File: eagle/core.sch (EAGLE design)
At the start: 28 parts, among them T1 BC846, T2 BC846, T3 BC846, T4 BC846

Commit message: Added capacitor between 3v and gnd on core pcb
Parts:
- added C3: 0.1u, resistor:C-EUC0805
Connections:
- net 3V: now also C3.1
- net GND: now also C3.2
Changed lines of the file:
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@@
 <part name="R11" library="resistor" library_urn="urn:adsk.eagle:library:348" deviceset="R-EU_" device="R0805" package3d_urn="urn:adsk.eagle:package:23553/2"/>
 <part name="R12" library="resistor" library_urn="urn:adsk.eagle:library:348" deviceset="R-EU_" device="R0805" package3d_urn="urn:adsk.eagle:package:23553/2"/>
+<part name="C3" library="resistor" library_urn="urn:adsk.eagle:library:348" deviceset="C-EU" device="C0805" package3d_urn="urn:adsk.eagle:package:23617/2" value="0.1u"/>
 </parts>
 <sheets>
@@
 <attribute name="VALUE" x="-22.098" y="13.97" size="1.778" layer="96" rot="R90"/>
 </instance>
+<instance part="C3" gate="G$1" x="20.32" y="30.48" smashed="yes">
+<attribute name="NAME" x="21.844" y="30.861" size="1.778" layer="95"/>
+<attribute name="VALUE" x="21.844" y="25.781" size="1.778" layer="96"/>
+</instance>
 </instances>
 <busses>
@@
 <wire x1="-144.78" y1="-27.94" x2="-139.7" y2="-27.94" width="0.1524" layer="91"/>
 <label x="-139.7" y="-27.94" size="1.778" layer="95"/>
+</segment>
+<segment>
+<pinref part="C3" gate="G$1" pin="2"/>
+<wire x1="20.32" y1="25.4" x2="25.4" y2="25.4" width="0.1524" layer="91"/>
+<label x="25.4" y="22.86" size="1.778" layer="95"/>
 </segment>
 </net>
@@
 <label x="-40.64" y="22.86" size="1.778" layer="95"/>
 </segment>
+<segment>
+<wire x1="20.32" y1="33.02" x2="15.24" y2="33.02" width="0.1524" layer="91"/>
+<pinref part="C3" gate="G$1" pin="1"/>
+<label x="12.7" y="33.02" size="1.778" layer="95"/>
+</segment>
 </net>

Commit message: Experimental fix for tft crash.
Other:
- note added: "I2C pullups"
- note removed: "Optional I2C pullups"
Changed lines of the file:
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@@
 <text x="-48.26" y="83.82" size="1.778" layer="91">Teensy 4</text>
 <text x="20.32" y="83.82" size="1.778" layer="91">Teensy 3.2</text>
-<text x="-40.64" y="25.4" size="1.778" layer="91">Optional I2C pullups</text>
+<text x="-40.64" y="25.4" size="1.778" layer="91">I2C pullups</text>
 </plain>
 <instances>

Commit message: misc pcb changes
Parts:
- removed C1, C2: 0.1u, resistor:C-EUC0805
- removed R10, R5, R8, R9: 10k, resistor:R-EU_M0805
- added GND: TPTP14R, testpad:TPTP14R
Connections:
- removed net ENCL: ENCL.TP, R5.2, R8.1
- removed net ENCR: ENCR.TP, R10.2, R9.1
- net 3V: no longer R8.2, R9.2
- net ENCPINL: now also ENCL.TP; no longer C1.1, R5.1
- net ENCPINR: now also ENCR.TP; no longer C2.1, R10.1
- net GND: now also GND.TP; no longer C1.2, C2.2
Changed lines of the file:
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@@
 </classes>
 <parts>
-<part name="R5" library="resistor" library_urn="urn:adsk.eagle:library:348" deviceset="R-EU_" device="M0805" package3d_urn="urn:adsk.eagle:package:23556/2" value="10k"/>
-<part name="R8" library="resistor" library_urn="urn:adsk.eagle:library:348" deviceset="R-EU_" device="M0805" package3d_urn="urn:adsk.eagle:package:23556/2" value="10k"/>
-<part name="R9" library="resistor" library_urn="urn:adsk.eagle:library:348" deviceset="R-EU_" device="M0805" package3d_urn="urn:adsk.eagle:package:23556/2" value="10k"/>
-<part name="R10" library="resistor" library_urn="urn:adsk.eagle:library:348" deviceset="R-EU_" device="M0805" package3d_urn="urn:adsk.eagle:package:23556/2" value="10k"/>
-<part name="C1" library="resistor" library_urn="urn:adsk.eagle:library:348" deviceset="C-EU" device="C0805" package3d_urn="urn:adsk.eagle:package:23617/2" value="0.1u"/>
-<part name="C2" library="resistor" library_urn="urn:adsk.eagle:library:348" deviceset="C-EU" device="C0805" package3d_urn="urn:adsk.eagle:package:23617/2" value="0.1u"/>
 <part name="U$1" library="general" deviceset="TEENSYSMALL" device="" value="TEENSY4"/>
 <part name="U$2" library="general" deviceset="TEENSYSMALL" device=""/>
@@
 <part name="R12" library="resistor" library_urn="urn:adsk.eagle:library:348" deviceset="R-EU_" device="R0805" package3d_urn="urn:adsk.eagle:package:23553/2"/>
 <part name="C3" library="resistor" library_urn="urn:adsk.eagle:library:348" deviceset="C-EU" device="C0805" package3d_urn="urn:adsk.eagle:package:23617/2" value="0.1u"/>
+<part name="GND" library="testpad" library_urn="urn:adsk.eagle:library:385" deviceset="TP" device="TP14R" package3d_urn="urn:adsk.eagle:package:27966/1"/>
 </parts>
 <sheets>
@@
 </plain>
 <instances>
-<instance part="R5" gate="G$1" x="-149.86" y="40.64" smashed="yes">
-<attribute name="NAME" x="-153.67" y="42.1386" size="1.778" layer="95"/>
-<attribute name="VALUE" x="-148.59" y="42.418" size="1.778" layer="96"/>
-</instance>
-<instance part="R8" gate="G$1" x="-139.7" y="45.72" smashed="yes" rot="R90">
-<attribute name="NAME" x="-141.1986" y="41.91" size="1.778" layer="95" rot="R90"/>
-<attribute name="VALUE" x="-141.478" y="46.99" size="1.778" layer="96" rot="R90"/>
-</instance>
-<instance part="R9" gate="G$1" x="-132.08" y="45.72" smashed="yes" rot="R90">
-<attribute name="NAME" x="-133.5786" y="41.91" size="1.778" layer="95" rot="R90"/>
-<attribute name="VALUE" x="-133.858" y="46.99" size="1.778" layer="96" rot="R90"/>
-</instance>
-<instance part="R10" gate="G$1" x="-121.92" y="40.64" smashed="yes" rot="R180">
-<attribute name="NAME" x="-118.11" y="39.1414" size="1.778" layer="95" rot="R180"/>
-<attribute name="VALUE" x="-123.19" y="38.862" size="1.778" layer="96" rot="R180"/>
-</instance>
-<instance part="C1" gate="G$1" x="-154.94" y="35.56" smashed="yes">
-<attribute name="NAME" x="-153.416" y="35.941" size="1.778" layer="95"/>
-<attribute name="VALUE" x="-153.416" y="30.861" size="1.778" layer="96"/>
-</instance>
-<instance part="C2" gate="G$1" x="-116.84" y="35.56" smashed="yes">
-<attribute name="NAME" x="-115.316" y="35.941" size="1.778" layer="95"/>
-<attribute name="VALUE" x="-115.316" y="30.861" size="1.778" layer="96"/>
-</instance>
 <instance part="U$1" gate="G$1" x="-43.18" y="60.96" smashed="yes"/>
 <instance part="U$2" gate="G$1" x="25.4" y="60.96" smashed="yes"/>
@@
 <attribute name="VALUE" x="21.844" y="25.781" size="1.778" layer="96"/>
 </instance>
+<instance part="GND" gate="G$1" x="-142.24" y="-30.48" smashed="yes" rot="R180">
+<attribute name="NAME" x="-140.97" y="-31.75" size="1.778" layer="95" rot="R180"/>
+<attribute name="TP_SIGNAL_NAME" x="-143.51" y="-29.21" size="1.778" layer="97" rot="R180"/>
+</instance>
 </instances>
 <busses>
@@
 <net name="GND" class="1">
 <segment>
-<pinref part="C1" gate="G$1" pin="2"/>
-<wire x1="-154.94" y1="30.48" x2="-154.94" y2="25.4" width="0.1524" layer="91"/>
-<label x="-154.94" y="25.4" size="1.778" layer="95"/>
-</segment>
-<segment>
-<pinref part="C2" gate="G$1" pin="2"/>
-<wire x1="-116.84" y1="30.48" x2="-116.84" y2="25.4" width="0.1524" layer="91"/>
-<label x="-116.84" y="25.4" size="1.778" layer="95"/>
-</segment>
-<segment>
 <pinref part="U$1" gate="G$1" pin="GND"/>
 <wire x1="-58.42" y1="78.74" x2="-66.04" y2="78.74" width="0.1524" layer="91"/>
@@
 <segment>
 <pinref part="R7" gate="G$1" pin="1"/>
-<wire x1="-144.78" y1="-27.94" x2="-139.7" y2="-27.94" width="0.1524" layer="91"/>
+<wire x1="-144.78" y1="-27.94" x2="-142.24" y2="-27.94" width="0.1524" layer="91"/>
 <label x="-139.7" y="-27.94" size="1.778" layer="95"/>
+<pinref part="GND" gate="G$1" pin="TP"/>
+<wire x1="-142.24" y1="-27.94" x2="-139.7" y2="-27.94" width="0.1524" layer="91"/>
+<junction x="-142.24" y="-27.94"/>
 </segment>
 <segment>
@@
 </net>
 <net name="3V" class="1">
-<segment>
-<pinref part="R8" gate="G$1" pin="2"/>
-<wire x1="-139.7" y1="50.8" x2="-139.7" y2="55.88" width="0.1524" layer="91"/>
-<wire x1="-139.7" y1="55.88" x2="-132.08" y2="55.88" width="0.1524" layer="91"/>
-<pinref part="R9" gate="G$1" pin="2"/>
-<wire x1="-132.08" y1="55.88" x2="-127" y2="55.88" width="0.1524" layer="91"/>
-<wire x1="-132.08" y1="50.8" x2="-132.08" y2="55.88" width="0.1524" layer="91"/>
-<junction x="-132.08" y="55.88"/>
-<label x="-127" y="55.88" size="1.778" layer="95"/>
-</segment>
 <segment>
 <pinref part="U$1" gate="G$1" pin="3V"/>
@@
 </segment>
 </net>
-<net name="ENCL" class="0">
-<segment>
-<pinref part="R8" gate="G$1" pin="1"/>
-<pinref part="R5" gate="G$1" pin="2"/>
-<wire x1="-144.78" y1="40.64" x2="-139.7" y2="40.64" width="0.1524" layer="91"/>
+<net name="ENCPINL" class="0">
+<segment>
+<wire x1="-139.7" y1="40.64" x2="-144.78" y2="40.64" width="0.1524" layer="91"/>
+<label x="-152.4" y="41.148" size="1.778" layer="95"/>
 <pinref part="ENCL" gate="G$1" pin="TP"/>
-<junction x="-139.7" y="40.64"/>
-</segment>
-</net>
-<net name="ENCR" class="0">
-<segment>
-<pinref part="R9" gate="G$1" pin="1"/>
-<pinref part="R10" gate="G$1" pin="2"/>
-<wire x1="-127" y1="40.64" x2="-132.08" y2="40.64" width="0.1524" layer="91"/>
-<pinref part="ENCR" gate="G$1" pin="TP"/>
-<junction x="-132.08" y="40.64"/>
-</segment>
-</net>
-<net name="ENCPINL" class="0">
-<segment>
-<pinref part="R5" gate="G$1" pin="1"/>
-<wire x1="-154.94" y1="40.64" x2="-160.02" y2="40.64" width="0.1524" layer="91"/>
-<label x="-167.64" y="41.148" size="1.778" layer="95"/>
-<pinref part="C1" gate="G$1" pin="1"/>
-<wire x1="-154.94" y1="38.1" x2="-154.94" y2="40.64" width="0.1524" layer="91"/>
-<junction x="-154.94" y="40.64"/>
 </segment>
 <segment>
@@
 <net name="ENCPINR" class="0">
 <segment>
-<pinref part="R10" gate="G$1" pin="1"/>
-<wire x1="-116.84" y1="40.64" x2="-111.76" y2="40.64" width="0.1524" layer="91"/>
-<label x="-114.3" y="41.148" size="1.778" layer="95"/>
-<pinref part="C2" gate="G$1" pin="1"/>
-<wire x1="-116.84" y1="38.1" x2="-116.84" y2="40.64" width="0.1524" layer="91"/>
-<junction x="-116.84" y="40.64"/>
-</segment>
-<segment>
+<wire x1="-132.08" y1="40.64" x2="-127" y2="40.64" width="0.1524" layer="91"/>
+<label x="-129.54" y="41.148" size="1.778" layer="95"/>
+<pinref part="ENCR" gate="G$1" pin="TP"/>
+</segment>
+<segment>

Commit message: all the things
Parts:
- removed R15, R16, R17, R18: (no value), resistor:R-EU_R0805
- removed T1, T2, T3, T4: BC846, transistor:BC846
- added SPGND, SPSCL, SPSDA, SPV: TPTP14R, testpad:TPTP14R
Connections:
- removed net N$2: R15.2, T1.B
- removed net N$3: R16.2, T2.B
- removed net N$4: R17.2, T3.B
- removed net N$5: R18.2, T4.B
- removed net PWM1: R15.1, U$1.2
- removed net PWM2: R16.1, U$1.3
- removed net PWM3: R17.1, U$1.4
- removed net PWM4: R18.1, U$1.5
- net 3V: now also SPV.TP
- net GND: now also SPGND.TP; no longer T1.E, T2.E, T3.E, T4.E
- net L1-: now also U$1.2; no longer T1.C
- net L2-: now also U$1.3; no longer T2.C
- net L3-: now also U$1.4; no longer T3.C
- net L4-: now also U$1.5; no longer T4.C
- net SCL: now also SPSCL.TP
- net SDA: now also SPSDA.TP

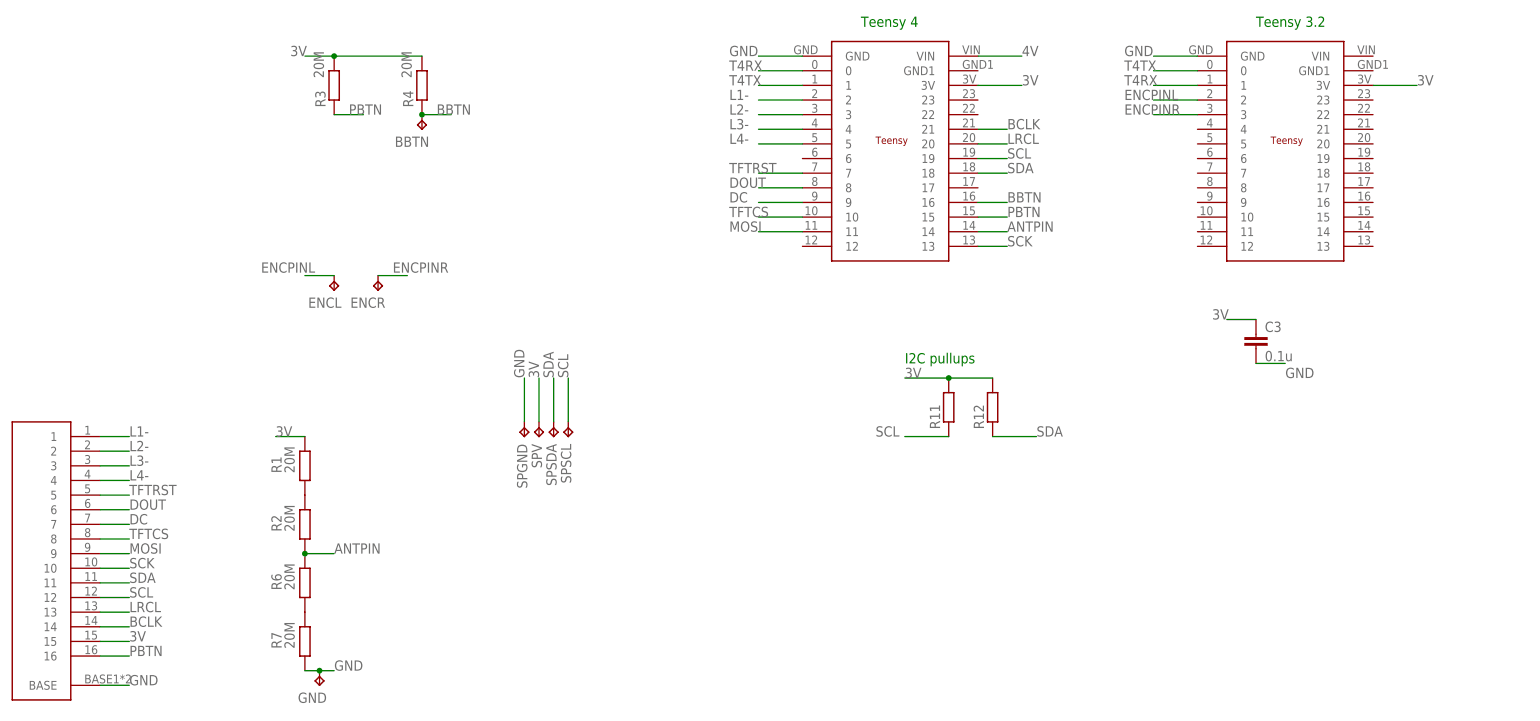
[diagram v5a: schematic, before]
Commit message: Added altimeter code
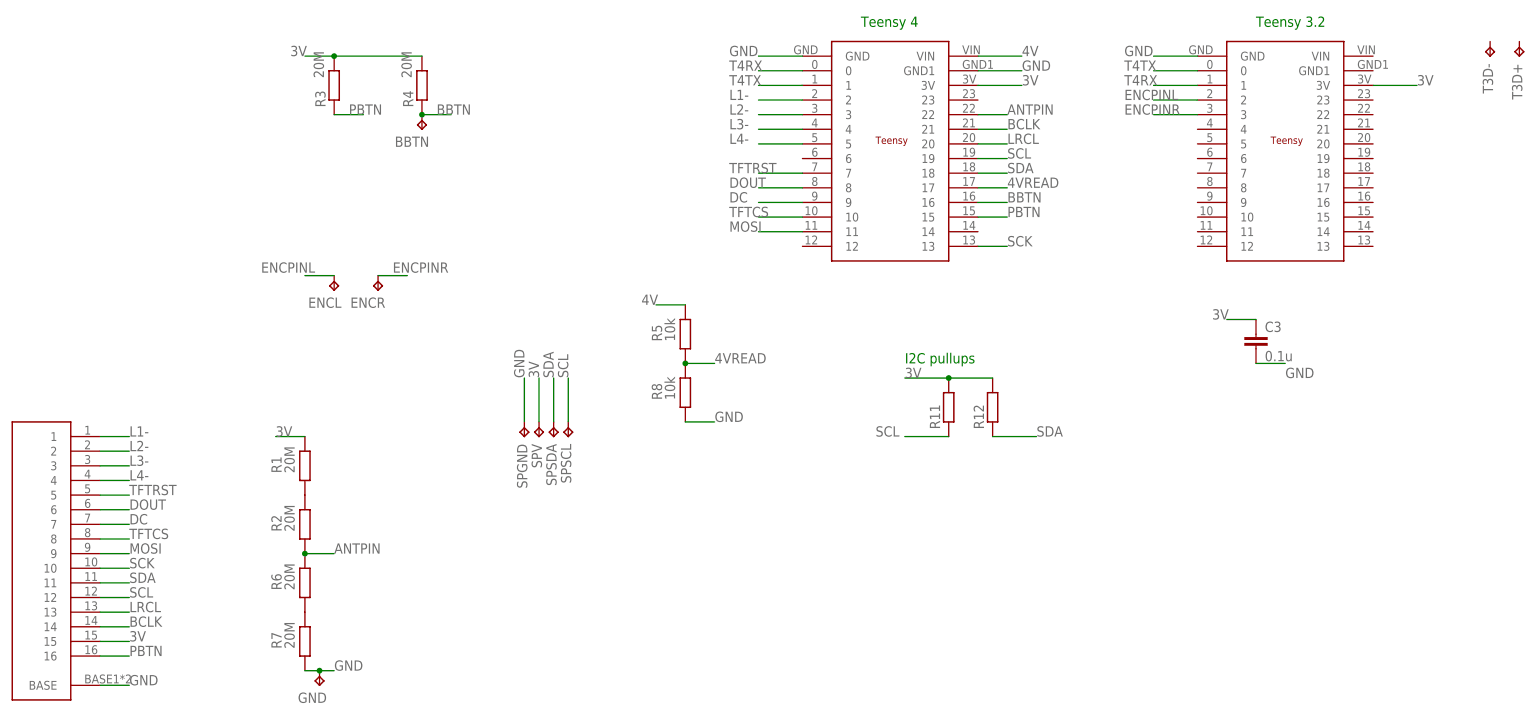
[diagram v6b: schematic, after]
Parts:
- added R5, R8: 10k, resistor:R-EU_M0805
- added T3D+, T3D-: TPTP14R, testpad:TPTP14R
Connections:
- new net 4VREAD: R5.1, R8.2, U$1.17
- net 4V: now also R5.2
- net ANTPIN: now also U$1.22; no longer U$1.14
- net GND: now also R8.1, U$1.GND1
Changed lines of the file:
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@@
 <part name="SPSDA" library="testpad" library_urn="urn:adsk.eagle:library:385" deviceset="TP" device="TP14R" package3d_urn="urn:adsk.eagle:package:27966/1"/>
 <part name="SPSCL" library="testpad" library_urn="urn:adsk.eagle:library:385" deviceset="TP" device="TP14R" package3d_urn="urn:adsk.eagle:package:27966/1"/>
+<part name="T3D-" library="testpad" library_urn="urn:adsk.eagle:library:385" deviceset="TP" device="TP14R" package3d_urn="urn:adsk.eagle:package:27966/1"/>
+<part name="T3D+" library="testpad" library_urn="urn:adsk.eagle:library:385" deviceset="TP" device="TP14R" package3d_urn="urn:adsk.eagle:package:27966/1"/>
+<part name="R5" library="resistor" library_urn="urn:adsk.eagle:library:348" deviceset="R-EU_" device="M0805" package3d_urn="urn:adsk.eagle:package:23556/2" value="10k"/>
+<part name="R8" library="resistor" library_urn="urn:adsk.eagle:library:348" deviceset="R-EU_" device="M0805" package3d_urn="urn:adsk.eagle:package:23556/2" value="10k"/>
 </parts>
 <sheets>
@@
 <attribute name="TP_SIGNAL_NAME" x="-100.33" y="13.97" size="1.778" layer="97" rot="R180"/>
 </instance>
+<instance part="T3D-" gate="G$1" x="60.96" y="78.74" smashed="yes" rot="R180">
+<attribute name="NAME" x="59.69" y="77.47" size="1.778" layer="95" rot="R270"/>
+<attribute name="TP_SIGNAL_NAME" x="59.69" y="80.01" size="1.778" layer="97" rot="R180"/>
+</instance>
+<instance part="T3D+" gate="G$1" x="66.04" y="78.74" smashed="yes" rot="R180">
+<attribute name="NAME" x="64.77" y="77.47" size="1.778" layer="95" rot="R270"/>
+<attribute name="TP_SIGNAL_NAME" x="64.77" y="80.01" size="1.778" layer="97" rot="R180"/>
+</instance>
+<instance part="R5" gate="G$1" x="-78.74" y="30.48" smashed="yes" rot="R90">
+<attribute name="NAME" x="-82.7786" y="29.21" size="1.778" layer="95" rot="R90"/>
+<attribute name="VALUE" x="-80.518" y="29.21" size="1.778" layer="96" rot="R90"/>
+</instance>
+<instance part="R8" gate="G$1" x="-78.74" y="20.32" smashed="yes" rot="R90">
+<attribute name="NAME" x="-82.7786" y="19.05" size="1.778" layer="95" rot="R90"/>
+<attribute name="VALUE" x="-80.518" y="19.05" size="1.778" layer="96" rot="R90"/>
+</instance>
 </instances>
 <busses>
@@
 <label x="-106.68" y="22.86" size="1.778" layer="95" rot="R90"/>
 </segment>
+<segment>
+<pinref part="U$1" gate="G$1" pin="GND1"/>
+<wire x1="-27.94" y1="76.2" x2="-20.32" y2="76.2" width="0.1524" layer="91"/>
+<label x="-20.32" y="76.2" size="1.778" layer="95"/>
+</segment>
+<segment>
+<pinref part="R8" gate="G$1" pin="1"/>
+<wire x1="-78.74" y1="15.24" x2="-73.66" y2="15.24" width="0.1524" layer="91"/>
+<label x="-73.66" y="15.24" size="1.778" layer="95"/>
+</segment>
 </net>
 <net name="3V" class="1">
@@
 <label x="-20.32" y="78.74" size="1.778" layer="95"/>
 </segment>
+<segment>
+<pinref part="R5" gate="G$1" pin="2"/>
+<wire x1="-78.74" y1="35.56" x2="-83.82" y2="35.56" width="0.1524" layer="91"/>
+<label x="-86.36" y="35.56" size="1.778" layer="95"/>
+</segment>
 </net>
 <net name="ANTPIN" class="0">
-<segment>
-<pinref part="U$1" gate="G$1" pin="14"/>
-<wire x1="-27.94" y1="48.26" x2="-22.86" y2="48.26" width="0.1524" layer="91"/>
-<label x="-22.86" y="48.26" size="1.778" layer="95"/>
-</segment>
 <segment>
 <pinref part="R2" gate="G$1" pin="1"/>
@@
 <label x="-139.7" y="-7.62" size="1.778" layer="95"/>
 </segment>
+<segment>
+<pinref part="U$1" gate="G$1" pin="22"/>
+<wire x1="-27.94" y1="68.58" x2="-22.86" y2="68.58" width="0.1524" layer="91"/>
+<label x="-22.86" y="68.58" size="1.778" layer="95"/>
+</segment>
 </net>
 <net name="BCLK" class="0">
@@
 </segment>
 </net>
+<net name="4VREAD" class="0">
+<segment>
+<pinref part="R5" gate="G$1" pin="1"/>
+<pinref part="R8" gate="G$1" pin="2"/>
+<wire x1="-78.74" y1="25.4" x2="-73.66" y2="25.4" width="0.1524" layer="91"/>
+<junction x="-78.74" y="25.4"/>
+<label x="-73.66" y="25.4" size="1.778" layer="95"/>
+</segment>
+<segment>
+<pinref part="U$1" gate="G$1" pin="17"/>
+<wire x1="-27.94" y1="55.88" x2="-22.86" y2="55.88" width="0.1524" layer="91"/>
+<label x="-22.86" y="55.88" size="1.778" layer="95"/>
+</segment>
+</net>
